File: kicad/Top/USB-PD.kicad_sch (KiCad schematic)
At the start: 42 parts

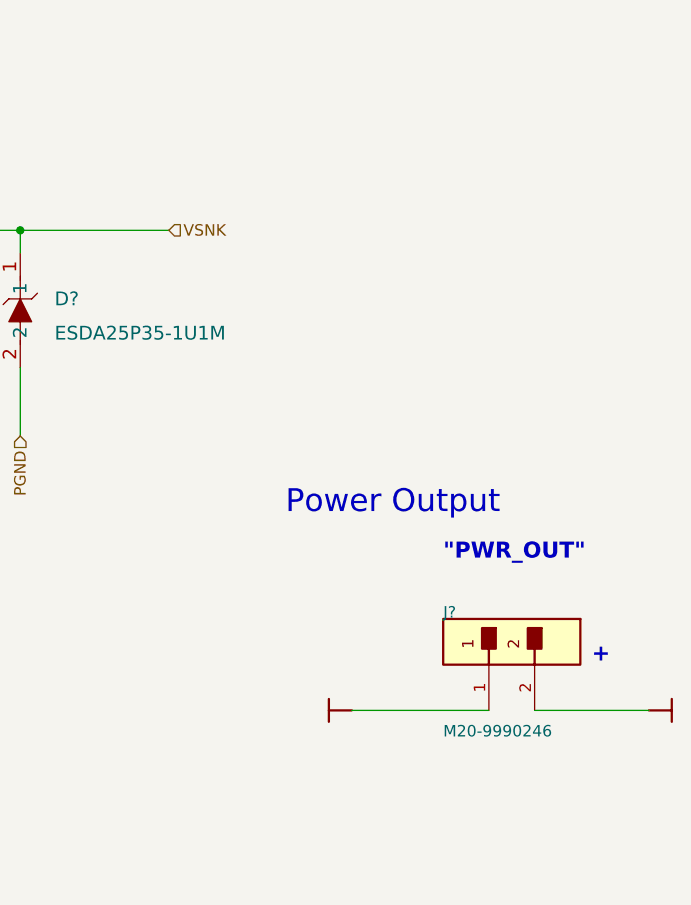
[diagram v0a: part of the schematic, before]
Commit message: Connected header to Vsnk
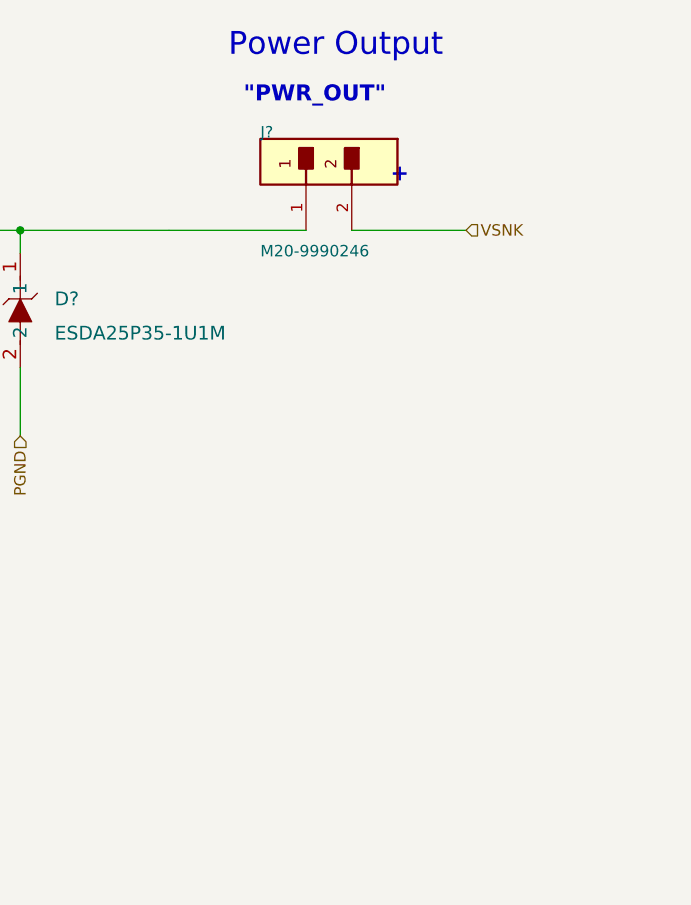
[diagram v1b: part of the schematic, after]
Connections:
- net VBUS_USB_OUT is gone; now on net VSNK: J?.2
- net VSNK: no longer C?.1, D?.1, Q?.5 (D), Q?.6 (D), Q?.7 (D), Q?.8 (D), R?.2
- net VBUS_USB: no longer names the net of J?.1
- net VBUS_USB: now also C?.1, D?.1, Q?.5 (D), Q?.6 (D), Q?.7 (D), Q?.8 (D), R?.2
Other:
- moved on the sheet: J?
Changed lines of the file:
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@@
     (stroke (width 0) (type default) (color 0 0 0 0))
   )
-  (wire (pts (xy 669.29 354.33) (xy 684.53 354.33))
+  (wire (pts (xy 648.97 300.99) (xy 664.21 300.99))
     (stroke (width 0.254) (type default) (color 0 0 0 0))
   )
@@
     (stroke (width 0.254) (type default) (color 0 0 0 0))
   )
-  (wire (pts (xy 689.61 354.33) (xy 702.31 354.33))
+  (wire (pts (xy 669.29 300.99) (xy 681.99 300.99))
     (stroke (width 0.254) (type default) (color 0 0 0 0))
   )
@@
     (stroke (width 0) (type default) (color 0 0 0 0))
   )
-  (text "+" (at 695.96 349.25 180)
-    (effects (font (size 1.778 1.778) bold) (justify left bottom))
+  (text "+" (at 675.64 295.91 180)
+    (effects (font (size 1.778 1.778) bold) (justify right bottom))
   )
   (text "\"PWR_IN\"" (at 393.7 286.8422 180)
     (effects (font (size 1.778 1.778) bold) (justify left bottom))
   )
-  (text "\"PWR_OUT\"" (at 679.45 337.82 180)
-    (effects (font (size 1.778 1.778) bold) (justify left bottom))
+  (text "\"PWR_OUT\"" (at 673.1 287.02 180)
+    (effects (font (size 1.778 1.778) bold) (justify right bottom))
   )
   (text "PWR" (at 577.85 295.7322 180)
     (effects (font (size 2.54 2.54) bold) (justify left bottom))
   )
-  (text "Power Output" (at 685.8 332.74 180)
+  (text "Power Output" (at 679.45 281.94 180)
     (effects (font (size 2.54 2.54)) (justify right bottom))
   )
@@
     (effects (font (size 1.27 1.27)) (justify left))
   )
-  (hierarchical_label "VSNK" (shape input) (at 648.97 300.99 0)
-    (effects (font (size 1.27 1.27)) (justify left))
-  )
   (hierarchical_label "PGND" (shape input) (at 632.46 323.85 270)
     (effects (font (size 1.27 1.27)) (justify right))
@@
   )
   (hierarchical_label "D-" (shape input) (at 427.99 346.71 0)
+    (effects (font (size 1.27 1.27)) (justify left))
+  )
+  (hierarchical_label "VSNK" (shape input) (at 681.99 300.99 0)
     (effects (font (size 1.27 1.27)) (justify left))
   )
@@
     (pin "1")
   )
-  (symbol (lib_id "Top-altium-import:3_mirrored_3bc925449376181038e59eaffc5286c") (at 684.53 354.33 0) (unit 1)
-    (in_bom yes) (on_board yes)
-    (property "Reference" "J?" (id 0) (at 679.45 344.17 0)
-      (effects (font (size 1.27 1.27)) (justify left bottom))
-    )
-    (property "Value" "M20-9990246" (id 1) (at 679.45 357.378 0)
-      (effects (font (size 1.27 1.27)) (justify left bottom))
-    )
-    (property "Footprint" "AltiumImports:FP-M20-9990246-MFG" (id 2) (at 684.53 354.33 0)
-      (effects (font (size 1.27 1.27)) hide)
-    )
-    (property "Datasheet" "" (id 3) (at 684.53 354.33 0)
+  (symbol (lib_id "Top-altium-import:3_mirrored_3bc925449376181038e59eaffc5286c") (at 664.21 300.99 0) (unit 1)
+    (in_bom yes) (on_board yes)
+    (property "Reference" "J?" (id 0) (at 659.13 290.83 0)
+      (effects (font (size 1.27 1.27)) (justify left bottom))
+    )
+    (property "Value" "M20-9990246" (id 1) (at 659.13 304.038 0)
+      (effects (font (size 1.27 1.27)) (justify left bottom))
+    )
+    (property "Footprint" "AltiumImports:FP-M20-9990246-MFG" (id 2) (at 664.21 300.99 0)
+      (effects (font (size 1.27 1.27)) hide)
+    )
+    (property "Datasheet" "" (id 3) (at 664.21 300.99 0)
       (effects (font (size 1.27 1.27)) hide)
     )
@@
     (pin "1")
   )
-  (symbol (lib_id "Top-altium-import:VBUS_USB") (at 669.29 354.33 270) (unit 1)
-    (in_bom yes) (on_board yes)
-    (property "Reference" "#PWR?" (id 0) (at 669.29 354.33 0)
-      (effects (font (size 1.27 1.27)) hide)
-    )
-    (property "Value" "~" (id 1) (at 665.48 354.33 90)
-      (effects (font (size 1.27 1.27)) (justify right))
-    )
-    (property "Footprint" "" (id 2) (at 669.29 354.33 0)
-      (effects (font (size 1.27 1.27)) hide)
-    )
-    (property "Datasheet" "" (id 3) (at 669.29 354.33 0)
-      (effects (font (size 1.27 1.27)) hide)
-    )
-    (pin "")
-  )
   (symbol (lib_id "Device:R_Small_US") (at 596.9 444.5 180) (unit 1)
     (in_bom yes) (on_board yes)
@@
     (pin "2")
   )
-  (symbol (lib_id "Top-altium-import:VBUS_USB_OUT") (at 702.31 354.33 90) (unit 1)
-    (in_bom yes) (on_board yes)
-    (property "Reference" "#PWR?" (id 0) (at 702.31 354.33 0)
-      (effects (font (size 1.27 1.27)) hide)
-    )
-    (property "Value" "~" (id 1) (at 706.12 354.33 90)
-      (effects (font (size 1.27 1.27)) (justify right))
-    )
-    (property "Footprint" "" (id 2) (at 702.31 354.33 0)
-      (effects (font (size 1.27 1.27)) hide)
-    )
-    (property "Datasheet" "" (id 3) (at 702.31 354.33 0)
-      (effects (font (size 1.27 1.27)) hide)
-    )
-    (pin "")
-  )
   (symbol (lib_id "Device:C_Small") (at 505.46 372.11 90) (unit 1)

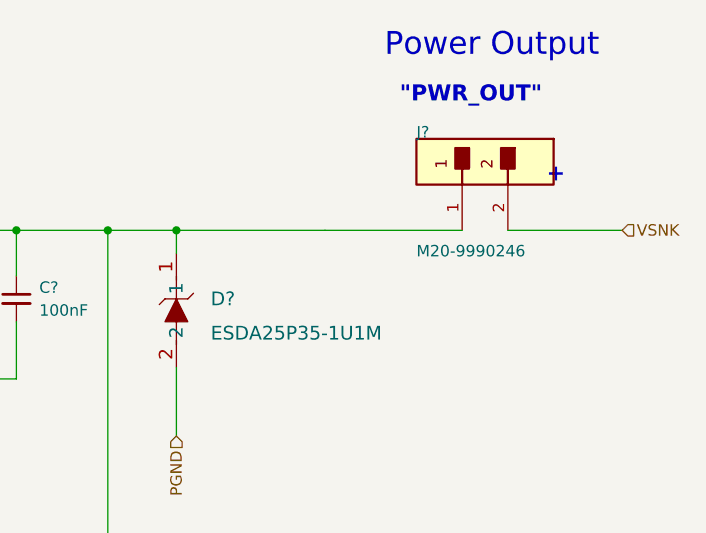
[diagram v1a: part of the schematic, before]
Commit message: Added jumper to vsnk
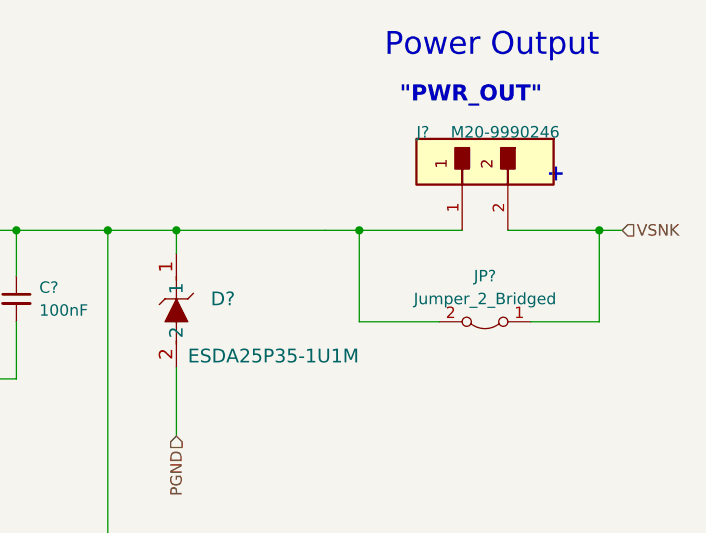
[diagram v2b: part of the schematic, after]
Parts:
- added JP?: Jumper_2_Bridged, symbol Jumper:Jumper_2_Bridged
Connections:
- net VSNK: now also JP?.1 (A)
- net at C?.1, D?.1, J?.1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: now also JP?.2 (B)
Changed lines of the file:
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@@
   (junction (at 443.23 459.74) (diameter 0) (color 0 0 0 0)
   )
+  (junction (at 652.78 300.99) (diameter 0) (color 0 0 0 0)
+  )
   (junction (at 497.84 375.92) (diameter 0) (color 0 0 0 0)
   )
@@
   )
   (junction (at 448.31 411.48) (diameter 0) (color 0 0 0 0)
+  )
+  (junction (at 679.45 300.99) (diameter 0) (color 0 0 0 0)
   )
   (junction (at 480.06 300.99) (diameter 0) (color 0 0 0 0)
@@
     (stroke (width 0) (type default) (color 0 0 0 0))
   )
+  (wire (pts (xy 652.78 300.99) (xy 664.21 300.99))
+    (stroke (width 0.254) (type default) (color 0 0 0 0))
+  )
   (wire (pts (xy 596.9 450.85) (xy 596.9 447.04))
     (stroke (width 0) (type default) (color 0 0 0 0))
   )
+  (wire (pts (xy 652.78 311.15) (xy 652.78 300.99))
+    (stroke (width 0) (type default) (color 0 0 0 0))
+  )
   (wire (pts (xy 444.5 361.95) (xy 435.61 361.95))
     (stroke (width 0.254) (type default) (color 0 0 0 0))
@@
   )
   (wire (pts (xy 580.39 435.61) (xy 580.39 450.85))
+    (stroke (width 0) (type default) (color 0 0 0 0))
+  )
+  (wire (pts (xy 679.45 311.15) (xy 679.45 300.99))
     (stroke (width 0) (type default) (color 0 0 0 0))
   )
@@
     (stroke (width 0) (type default) (color 0 0 0 0))
   )
+  (wire (pts (xy 661.67 311.15) (xy 652.78 311.15))
+    (stroke (width 0) (type default) (color 0 0 0 0))
+  )
   (polyline (pts (xy 588.01 297.18) (xy 586.74 295.91))
     (stroke (width 0.254) (type solid) (color 0 0 0 0))
@@
     (stroke (width 0) (type default) (color 0 0 0 0))
   )
-  (wire (pts (xy 648.97 300.99) (xy 664.21 300.99))
+  (wire (pts (xy 648.97 300.99) (xy 652.78 300.99))
     (stroke (width 0.254) (type default) (color 0 0 0 0))
   )
@@
     (stroke (width 0.254) (type default) (color 0 0 0 0))
   )
+  (wire (pts (xy 679.45 300.99) (xy 681.99 300.99))
+    (stroke (width 0.254) (type default) (color 0 0 0 0))
+  )
   (wire (pts (xy 448.31 359.41) (xy 448.31 411.48))
     (stroke (width 0.254) (type default) (color 0 0 0 0))
@@
     (stroke (width 0.254) (type default) (color 0 0 0 0))
   )
-  (wire (pts (xy 669.29 300.99) (xy 681.99 300.99))
+  (wire (pts (xy 669.29 300.99) (xy 679.45 300.99))
     (stroke (width 0.254) (type default) (color 0 0 0 0))
   )
   (wire (pts (xy 416.56 351.79) (xy 425.45 351.79))
     (stroke (width 0.254) (type default) (color 0 0 0 0))
+  )
+  (wire (pts (xy 671.83 311.15) (xy 679.45 311.15))
+    (stroke (width 0) (type default) (color 0 0 0 0))
   )
   (wire (pts (xy 580.39 419.1) (xy 601.98 419.1))
@@
     (pin "3")
   )
+  (symbol (lib_id "Jumper:Jumper_2_Bridged") (at 666.75 311.15 180) (unit 1)
+    (in_bom yes) (on_board yes) (fields_autoplaced)
+    (property "Reference" "JP?" (id 0) (at 666.75 306.07 0))
+    (property "Value" "Jumper_2_Bridged" (id 1) (at 666.75 308.61 0))
+    (property "Footprint" "" (id 2) (at 666.75 311.15 0)
+      (effects (font (size 1.27 1.27)) hide)
+    )
+    (property "Datasheet" "~" (id 3) (at 666.75 311.15 0)
+      (effects (font (size 1.27 1.27)) hide)
+    )
+    (pin "1")
+    (pin "2")
+  )
   (symbol (lib_id "Device:R_Small_US") (at 443.23 457.2 0) (unit 1)
     (in_bom yes) (on_board yes)
@@
       (effects (font (size 1.27 1.27)) (justify left bottom))
     )
-    (property "Value" "M20-9990246" (id 1) (at 659.13 304.038 0)
+    (property "Value" "M20-9990246" (id 1) (at 662.94 290.83 0)
       (effects (font (size 1.27 1.27)) (justify left bottom))
     )
@@
   )
   (symbol (lib_id "ESDA25P35-1U1M:ESDA25P35-1U1M") (at 632.46 309.88 270) (unit 1)
-    (in_bom yes) (on_board yes) (fields_autoplaced)
+    (in_bom yes) (on_board yes)
     (property "Reference" "D?" (id 0) (at 636.27 308.61 90)
       (effects (font (size 1.524 1.524)) (justify left))
     )
-    (property "Value" "ESDA25P35-1U1M" (id 1) (at 636.27 312.42 90)
+    (property "Value" "ESDA25P35-1U1M" (id 1) (at 633.73 314.96 90)
       (effects (font (size 1.524 1.524)) (justify left))
     )

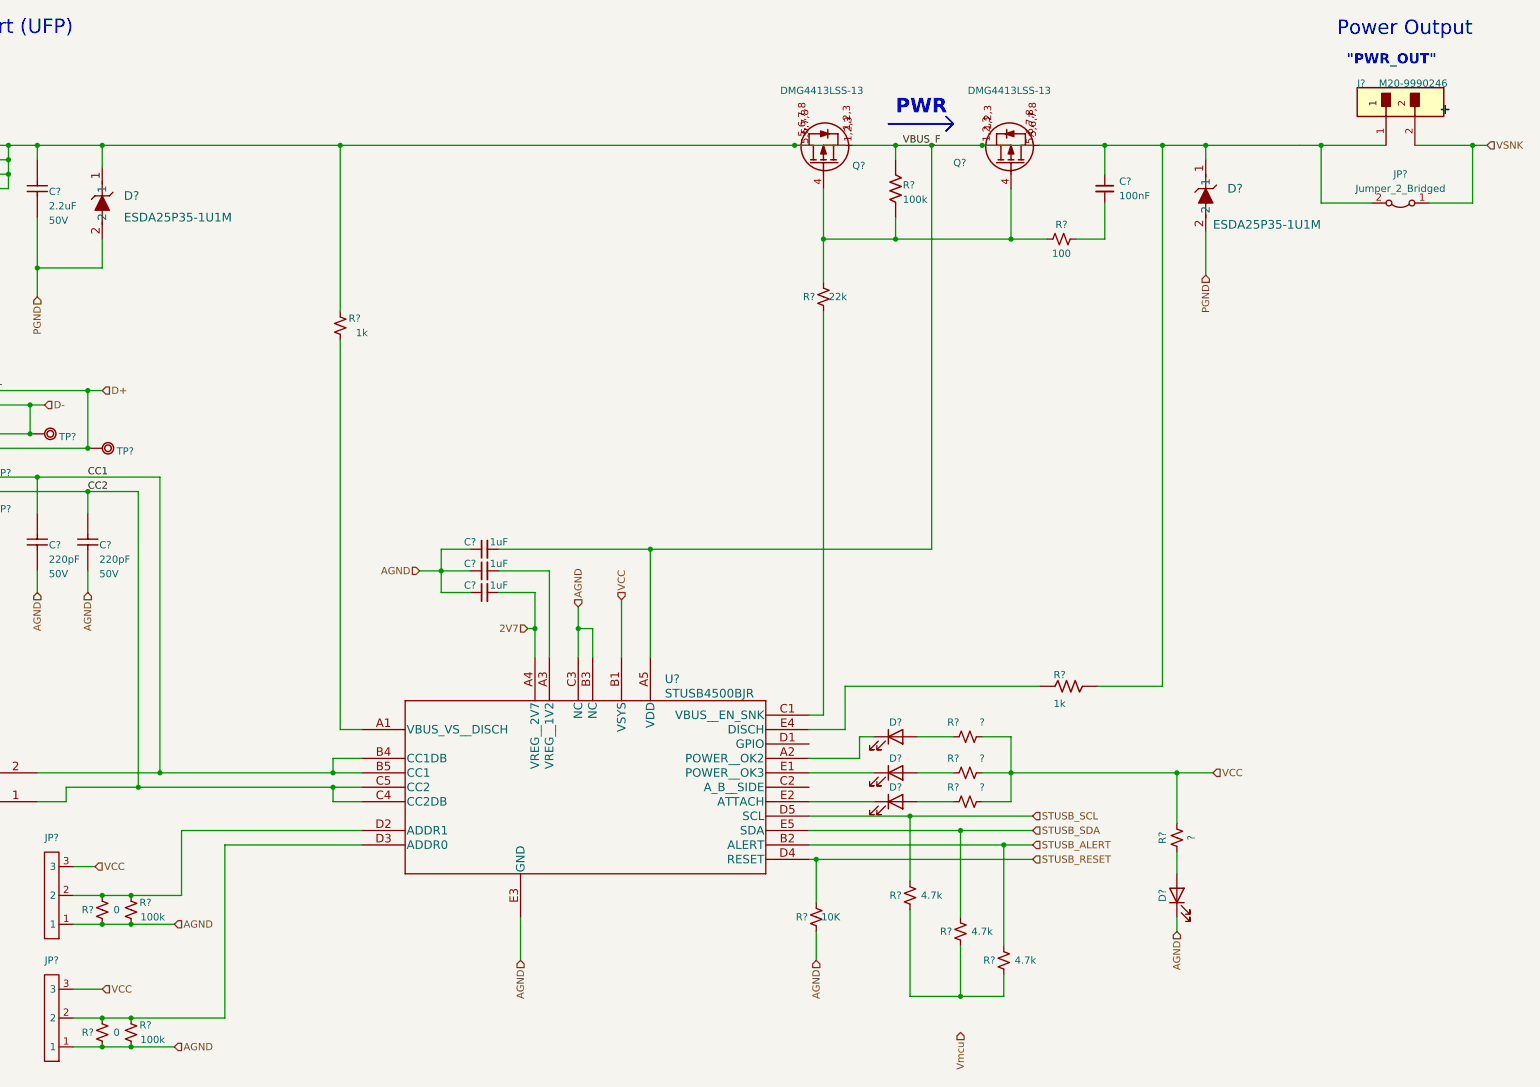
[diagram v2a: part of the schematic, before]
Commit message: Added missing Vmcu wire and cleaned things up
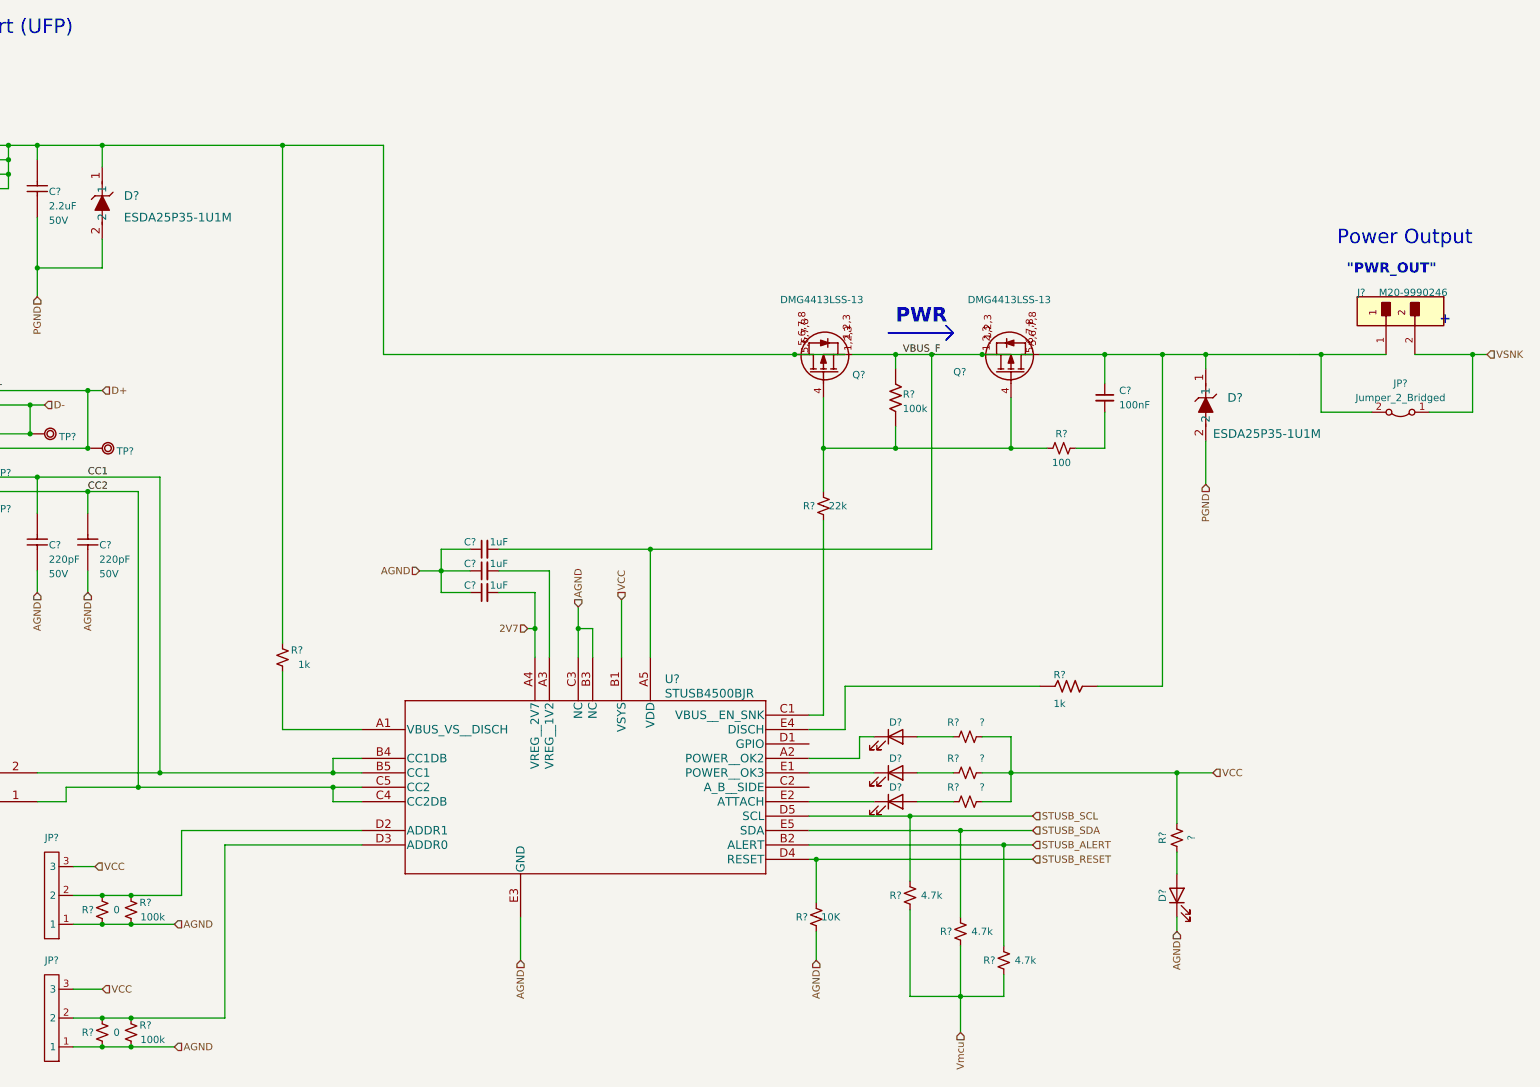
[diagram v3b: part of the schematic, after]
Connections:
- net Vmcu: now also R?.1, R?.1, R?.1
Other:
- moved on the sheet: C?, D?, J?, JP?, Q?, R?
